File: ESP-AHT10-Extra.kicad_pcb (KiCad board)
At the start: 2 copper layers, 38.2 x 20.8 mm, 23 parts, among them J1 USB, SW1 RESET, SW2 PROG, U1 CH330N, U2 HT7233, U3 ESP-12, U4 AHT10, U5 USBLC6-2SC6

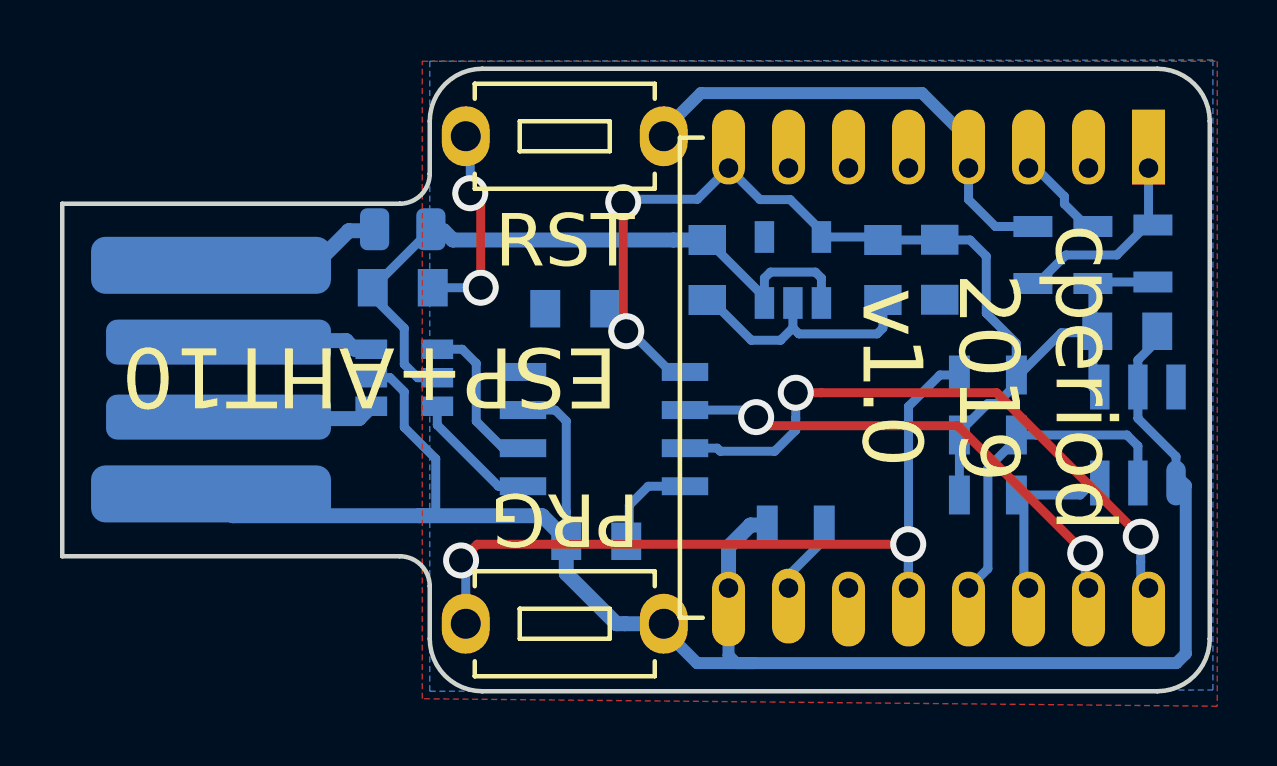
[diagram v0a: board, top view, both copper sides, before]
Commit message: drop vias to 0.6mm
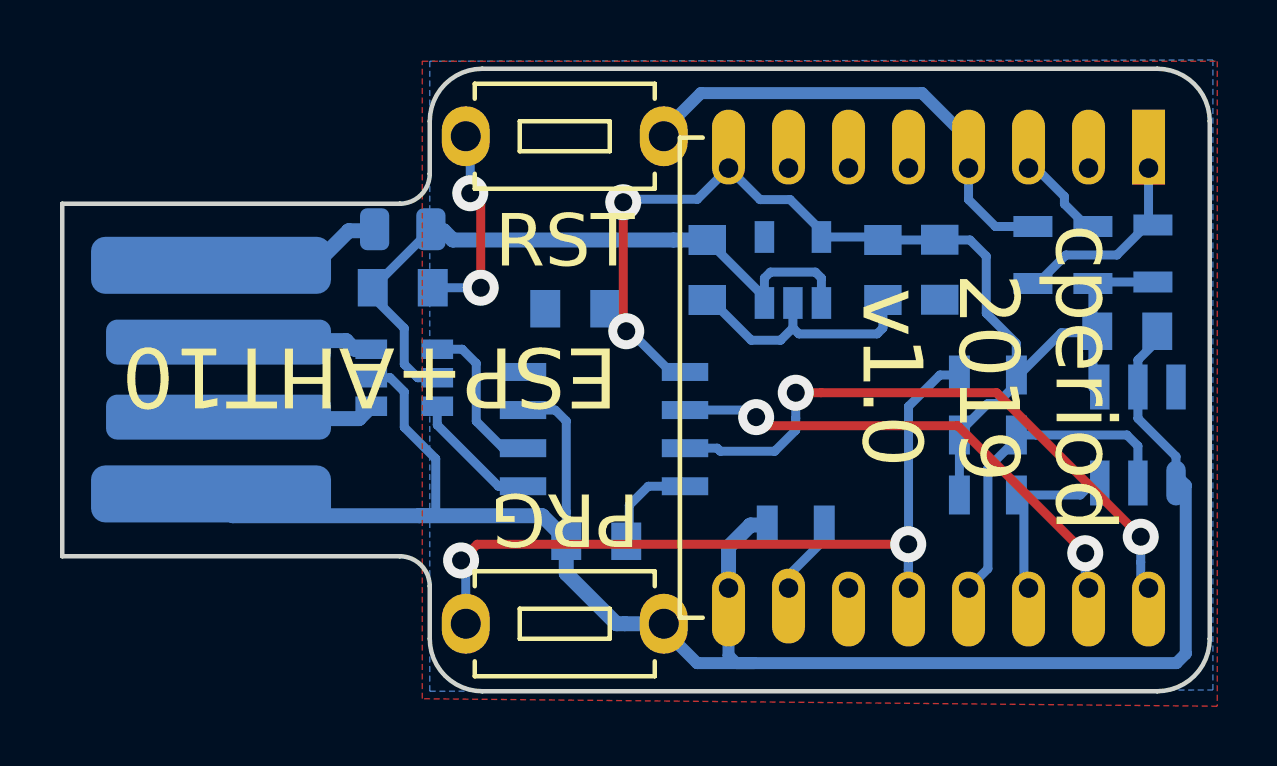
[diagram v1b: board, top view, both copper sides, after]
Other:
- net class Default: via_drill 0.8 -> 0.6
- rule via_min_drill: 0.8 -> 0.6
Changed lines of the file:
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@@
   (page A4)
   (layers
-    (0 F.Cu signal hide)
-    (31 B.Cu signal hide)
-    (32 B.Adhes user hide)
-    (33 F.Adhes user hide)
-    (34 B.Paste user hide)
-    (35 F.Paste user hide)
-    (36 B.SilkS user hide)
-    (37 F.SilkS user hide)
-    (38 B.Mask user hide)
-    (39 F.Mask user hide)
+    (0 F.Cu signal)
+    (31 B.Cu signal)
+    (32 B.Adhes user)
+    (33 F.Adhes user)
+    (34 B.Paste user)
+    (35 F.Paste user)
+    (36 B.SilkS user)
+    (37 F.SilkS user)
+    (38 B.Mask user)
+    (39 F.Mask user)
     (40 Dwgs.User user)
-    (41 Cmts.User user hide)
-    (42 Eco1.User user hide)
-    (43 Eco2.User user hide)
+    (41 Cmts.User user)
+    (42 Eco1.User user)
+    (43 Eco2.User user)
     (44 Edge.Cuts user)
-    (45 Margin user hide)
-    (46 B.CrtYd user hide)
-    (47 F.CrtYd user hide)
-    (48 B.Fab user hide)
-    (49 F.Fab user hide)
+    (45 Margin user)
+    (46 B.CrtYd user)
+    (47 F.CrtYd user)
+    (48 B.Fab user)
+    (49 F.Fab user)
   )
   (setup
@@
     (edge_width 0.15)
     (via_size 1.2)
-    (via_drill 0.8)
+    (via_drill 0.6)
     (via_min_size 1.2)
-    (via_min_drill 0.8)
+    (via_min_drill 0.6)
     (uvia_size 0.3)
     (uvia_drill 0.1)
@@
     (trace_width 0.3)
     (via_dia 1.2)
-    (via_drill 0.8)
+    (via_drill 0.6)
     (uvia_dia 0.3)
     (uvia_drill 0.1)
@@
   (segment (start 157.355703 92.70862) (end 160.25862 92.70862) (width 0.3) (layer B.Cu) (net 1))
   (segment (start 160.25862 92.70862) (end 160.8 93.25) (width 0.3) (layer B.Cu) (net 1))
-  (via (at 148.7 91.45) (size 1.2) (drill 0.8) (layers F.Cu B.Cu) (net 1))
+  (via (at 148.7 91.45) (size 1.2) (drill 0.6) (layers F.Cu B.Cu) (net 1))
   (segment (start 148.8 91.35) (end 148.7 91.45) (width 0.3) (layer B.Cu) (net 1))
   (segment (start 152.209217 90.312374) (end 151.171591 91.35) (width 0.3) (layer B.Cu) (net 1))
   (segment (start 151.171591 91.35) (end 148.8 91.35) (width 0.3) (layer B.Cu) (net 1))
-  (via (at 148.800042 95.75) (size 1.2) (drill 0.8) (layers F.Cu B.Cu) (net 1))
+  (via (at 148.800042 95.75) (size 1.2) (drill 0.6) (layers F.Cu B.Cu) (net 1))
   (segment (start 148.7 91.45) (end 148.7 95.649958) (width 0.3) (layer F.Cu) (net 1))
   (segment (start 148.7 95.649958) (end 148.800042 95.75) (width 0.3) (layer F.Cu) (net 1))
@@
   (segment (start 152.209217 104.312374) (end 152.209217 102.940783) (width 0.5) (layer B.Cu) (net 2))
   (segment (start 152.209217 102.940783) (end 152.94138 102.20862) (width 0.5) (layer B.Cu) (net 2))
-  (via (at 143.95 94.3) (size 1.2) (drill 0.8) (layers F.Cu B.Cu) (net 2))
+  (via (at 143.95 94.3) (size 1.2) (drill 0.6) (layers F.Cu B.Cu) (net 2))
   (segment (start 142.35 94.3) (end 143.95 94.3) (width 0.3) (layer B.Cu) (net 2))
-  (via (at 143.6 91.15) (size 1.2) (drill 0.8) (layers F.Cu B.Cu) (net 2))
+  (via (at 143.6 91.15) (size 1.2) (drill 0.6) (layers F.Cu B.Cu) (net 2))
   (segment (start 143.95 94.3) (end 143.95 91.5) (width 0.3) (layer F.Cu) (net 2))
   (segment (start 143.95 91.5) (end 143.6 91.15) (width 0.3) (layer F.Cu) (net 2))
@@
   (segment (start 158.209217 104.312374) (end 158.2 104.303157) (width 0.3) (layer B.Cu) (net 9))
   (segment (start 158.2 103.698528) (end 158.2 102.85) (width 0.3) (layer B.Cu) (net 9))
-  (via (at 158.2 102.85) (size 1.2) (drill 0.8) (layers F.Cu B.Cu) (net 9))
+  (via (at 158.2 102.85) (size 1.2) (drill 0.6) (layers F.Cu B.Cu) (net 9))
   (segment (start 158.2 104.303157) (end 158.2 103.698528) (width 0.3) (layer B.Cu) (net 9))
   (segment (start 158.2 102.85) (end 143.834321 102.85) (width 0.3) (layer F.Cu) (net 9))
@@
   (segment (start 143.45 103.545839) (end 143.294241 103.39008) (width 0.3) (layer B.Cu) (net 9))
   (segment (start 143.45 105.5) (end 143.45 103.545839) (width 0.3) (layer B.Cu) (net 9))
-  (via (at 143.294241 103.39008) (size 1.2) (drill 0.8) (layers F.Cu B.Cu) (net 9))
+  (via (at 143.294241 103.39008) (size 1.2) (drill 0.6) (layers F.Cu B.Cu) (net 9))
   (segment (start 161.805703 99.35862) (end 161.805703 99.20862) (width 0.3) (layer B.Cu) (net 10))
   (segment (start 160.855703 100.30862) (end 161.805703 99.35862) (width 0.3) (layer B.Cu) (net 10))
@@
   (segment (start 161.805703 101.20862) (end 163.935703 101.20862) (width 0.3) (layer B.Cu) (net 11))
   (segment (start 163.935703 101.20862) (end 164.585703 100.55862) (width 0.3) (layer B.Cu) (net 11))
-  (via (at 164.1 103.15) (size 1.2) (drill 0.8) (layers F.Cu B.Cu) (net 12))
+  (via (at 164.1 103.15) (size 1.2) (drill 0.6) (layers F.Cu B.Cu) (net 12))
   (segment (start 164.1 104.203157) (end 164.209217 104.312374) (width 0.3) (layer B.Cu) (net 12))
   (segment (start 164.1 103.15) (end 164.1 104.203157) (width 0.3) (layer B.Cu) (net 12))
@@
   (segment (start 164.1 103.15) (end 159.850002 98.900002) (width 0.3) (layer F.Cu) (net 12))
   (segment (start 153.417564 98.900002) (end 153.12992 98.612358) (width 0.3) (layer F.Cu) (net 12))
-  (via (at 153.12992 98.612358) (size 1.2) (drill 0.8) (layers F.Cu B.Cu) (net 12))
+  (via (at 153.12992 98.612358) (size 1.2) (drill 0.6) (layers F.Cu B.Cu) (net 12))
   (segment (start 165.95 103.448528) (end 165.95 102.6) (width 0.3) (layer B.Cu) (net 13))
   (segment (start 165.95 104.053157) (end 165.95 103.448528) (width 0.3) (layer B.Cu) (net 13))
   (segment (start 166.209217 104.312374) (end 165.95 104.053157) (width 0.3) (layer B.Cu) (net 13))
-  (via (at 165.95 102.6) (size 1.2) (drill 0.8) (layers F.Cu B.Cu) (net 13))
+  (via (at 165.95 102.6) (size 1.2) (drill 0.6) (layers F.Cu B.Cu) (net 13))
   (segment (start 154.45 99.048528) (end 154.45 98.648528) (width 0.3) (layer B.Cu) (net 13))
   (segment (start 161.15 97.8) (end 155.298528 97.8) (width 0.3) (layer F.Cu) (net 13))
@@
   (segment (start 155.298528 97.8) (end 154.45 97.8) (width 0.3) (layer F.Cu) (net 13))
   (segment (start 151.936845 99.750002) (end 153.748526 99.750002) (width 0.3) (layer B.Cu) (net 13))
-  (via (at 154.45 97.8) (size 1.2) (drill 0.8) (layers F.Cu B.Cu) (net 13))
+  (via (at 154.45 97.8) (size 1.2) (drill 0.6) (layers F.Cu B.Cu) (net 13))
   (segment (start 150.759217 99.647374) (end 151.834217 99.647374) (width 0.3) (layer B.Cu) (net 13))
   (segment (start 134.959217 93.552374) (end 138.397626 93.552374) (width 0.5) (layer B.Cu) (net 14))

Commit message: fix V3 connections to CH330N, bump the bulk caps to 10uF, rev number
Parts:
- C2: value 1u -> 10u
- C4: value 2.2u -> 10u
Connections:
- C6 pad 1: Net-(C6-Pad1) -> 3V3
- U1 pad 8: Net-(C6-Pad1) -> 3V3
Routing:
- net 3V3: track 40.0 -> 49.7 mm
- net Net-(C6-Pad1): track 3.35 -> 0.00 mm
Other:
- board text added: "cperiod 2019 v1.2"
- board text removed: "cperiod 2019 v1.0"
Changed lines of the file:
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@@
     (thickness 1.6)
     (drawings 18)
-    (tracks 201)
+    (tracks 203)
     (zones 0)
     (modules 23)
-    (nets 19)
+    (nets 18)
   )
   (page A4)
@@
   (net 15 UDP+)
   (net 16 UDP-)
-  (net 17 "Net-(C6-Pad1)")
-  (net 18 5V)
+  (net 17 5V)
   (net_class Default "This is the default net class."
     (clearance 0.35)
@@
     (add_net 5V)
     (add_net GND)
-    (add_net "Net-(C6-Pad1)")
     (add_net "Net-(R1-Pad2)")
     (add_net "Net-(R2-Pad1)")
@@
       (effects (font (size 1 1) (thickness 0.15)) (justify mirror))
     )
-    (fp_text value 1u (at -8.10862 0.3 270) (layer B.Fab)
+    (fp_text value 10u (at -8.45862 -0.25 270) (layer B.Fab)
       (effects (font (size 1 1) (thickness 0.15)) (justify mirror))
     )
@@
       (net 2 GND))
     (pad 1 smd rect (at -1 0 270) (size 1 1.25) (layers B.Cu B.Paste B.Mask)
-      (net 18 5V))
+      (net 17 5V))
     (model Capacitors_SMD.3dshapes/C_0805.wrl
       (at (xyz 0 0 0))
@@
       (effects (font (size 1 1) (thickness 0.15)) (justify mirror))
     )
-    (fp_text value 2.2u (at -8.75 0.25 270) (layer B.Fab)
+    (fp_text value 10u (at -8.75 0.25 270) (layer B.Fab)
       (effects (font (size 1 1) (thickness 0.15)) (justify mirror))
     )
@@
       (net 13 eTX))
     (pad 8 smd rect (at 2.7 1.905) (size 1.55 0.6) (layers B.Cu B.Paste B.Mask)
-      (net 17 "Net-(C6-Pad1)"))
+      (net 1 3V3))
     (model ${KISYS3DMOD}/Package_SO.3dshapes/SOIC-8_3.9x4.9mm_P1.27mm.wrl
       (at (xyz 0 0 0))
@@
     (fp_line (start 0.9 1.55) (end 0.9 -1.55) (layer B.Fab) (width 0.1))
     (pad 1 smd rect (at -1.1 0.95 90) (size 1.06 0.65) (layers B.Cu B.Paste B.Mask)
-      (net 18 5V))
+      (net 17 5V))
     (pad 2 smd rect (at -1.1 0 90) (size 1.06 0.65) (layers B.Cu B.Paste B.Mask)
       (net 2 GND))
     (pad 3 smd rect (at -1.1 -0.95 90) (size 1.06 0.65) (layers B.Cu B.Paste B.Mask)
-      (net 18 5V))
+      (net 17 5V))
     (pad 4 smd rect (at 1.1 -0.95 90) (size 1.06 0.65) (layers B.Cu B.Paste B.Mask))
     (pad 5 smd rect (at 1.1 0.95 90) (size 1.06 0.65) (layers B.Cu B.Paste B.Mask)
@@
       (net 2 GND))
     (pad 1 smd rect (at -1 0 180) (size 1 1.25) (layers B.Cu B.Paste B.Mask)
-      (net 17 "Net-(C6-Pad1)"))
+      (net 1 3V3))
     (model Capacitors_SMD.3dshapes/C_0805.wrl
       (at (xyz 0 0 0))
@@
       (net 15 UDP+))
     (pad 5 smd rect (at 1.1 0) (size 1.06 0.65) (layers B.Cu B.Paste B.Mask)
-      (net 18 5V))
+      (net 17 5V))
     (model ${KISYS3DMOD}/Package_TO_SOT_SMD.3dshapes/SOT-23-6.wrl
       (at (xyz 0 0 0))
@@
       (net 14 VBUS))
     (pad 1 smd roundrect (at -0.9375 0 180) (size 0.975 1.4) (layers B.Cu B.Paste B.Mask) (roundrect_rratio 0.25)
-      (net 18 5V))
+      (net 17 5V))
     (model ${KISYS3DMOD}/Fuse.3dshapes/Fuse_0805_2012Metric.wrl
       (at (xyz 0 0 0))
@@
       (net 2 GND))
     (pad 1 smd rect (at -1 0) (size 1 1.25) (layers B.Cu B.Paste B.Mask)
-      (net 18 5V))
+      (net 17 5V))
     (model Capacitors_SMD.3dshapes/C_0805.wrl
       (at (xyz 0 0 0))
@@
   (gr_line (start 130 103.25) (end 130 91.5) (layer Edge.Cuts) (width 0.15))
   (gr_line (start 141.25 103.25) (end 130 103.25) (layer Edge.Cuts) (width 0.15))
-  (gr_text "cperiod\n2019\nv1.0" (at 160.85 97.3 270) (layer F.SilkS)
+  (gr_text "cperiod\n2019\nv1.2" (at 160.85 97.3 270) (layer F.SilkS)
     (effects (font (size 2 2) (thickness 0.3)))
   )
@@
   (segment (start 143.8 98.75) (end 144.697374 99.647374) (width 0.3) (layer B.Cu) (net 16))
   (segment (start 143.33 96.35) (end 143.8 96.82) (width 0.3) (layer B.Cu) (net 16))
-  (segment (start 150.705703 100.970888) (end 150.759217 100.917374) (width 0.3) (layer B.Cu) (net 17))
-  (segment (start 149.532626 100.917374) (end 148.9 101.55) (width 0.3) (layer B.Cu) (net 17))
-  (segment (start 150.759217 100.917374) (end 149.532626 100.917374) (width 0.3) (layer B.Cu) (net 17))
-  (segment (start 148.9 101.55) (end 148.9 102.7) (width 0.3) (layer B.Cu) (net 17))
-  (segment (start 153.405703 94.614323) (end 153.405703 94.80862) (width 0.3) (layer B.Cu) (net 18))
-  (segment (start 151.5 92.70862) (end 153.405703 94.614323) (width 0.3) (layer B.Cu) (net 18))
-  (segment (start 155.105702 93.778619) (end 155.305703 93.97862) (width 0.3) (layer B.Cu) (net 18))
-  (segment (start 153.605704 93.778619) (end 155.105702 93.778619) (width 0.3) (layer B.Cu) (net 18))
-  (segment (start 155.305703 93.97862) (end 155.305703 94.80862) (width 0.3) (layer B.Cu) (net 18))
-  (segment (start 153.405703 93.97862) (end 153.605704 93.778619) (width 0.3) (layer B.Cu) (net 18))
-  (segment (start 153.405703 94.80862) (end 153.405703 93.97862) (width 0.3) (layer B.Cu) (net 18))
-  (segment (start 150.375 92.70862) (end 151.5 92.70862) (width 0.5) (layer B.Cu) (net 18))
-  (segment (start 142.125 92.4) (end 142.7125 92.4) (width 0.5) (layer B.Cu) (net 18))
-  (segment (start 142.7125 92.4) (end 143.02112 92.70862) (width 0.5) (layer B.Cu) (net 18))
-  (segment (start 143.02112 92.70862) (end 150.375 92.70862) (width 0.5) (layer B.Cu) (net 18))
-  (segment (start 142.125 92.525) (end 142.125 92.4) (width 0.3) (layer B.Cu) (net 18))
-  (segment (start 140.35 94.3) (end 142.125 92.525) (width 0.3) (layer B.Cu) (net 18))
-  (segment (start 141.4 95.65) (end 140.5 94.75) (width 0.3) (layer B.Cu) (net 18))
-  (segment (start 141.4 96.85) (end 141.4 95.65) (width 0.3) (layer B.Cu) (net 18))
-  (segment (start 140.5 94.75) (end 140.5 94.3) (width 0.3) (layer B.Cu) (net 18))
-  (segment (start 142.5 97.3) (end 141.85 97.3) (width 0.3) (layer B.Cu) (net 18))
-  (segment (start 141.85 97.3) (end 141.4 96.85) (width 0.3) (layer B.Cu) (net 18))
+  (segment (start 150.705703 100.970888) (end 150.759217 100.917374) (width 0.3) (layer B.Cu) (net 1))
+  (segment (start 150.759217 100.917374) (end 150.582626 100.917374) (width 0.3) (layer B.Cu) (net 1))
+  (segment (start 148.9 102.6) (end 148.9 102.7) (width 0.3) (layer B.Cu) (net 1))
+  (segment (start 150.582626 100.917374) (end 148.9 102.6) (width 0.3) (layer B.Cu) (net 1))
+  (segment (start 148.8 95.750042) (end 148.800042 95.75) (width 0.3) (layer B.Cu) (net 1))
+  (segment (start 148.8 102.75) (end 148.8 95.750042) (width 0.3) (layer B.Cu) (net 1))
+  (segment (start 153.405703 94.614323) (end 153.405703 94.80862) (width 0.3) (layer B.Cu) (net 17))
+  (segment (start 151.5 92.70862) (end 153.405703 94.614323) (width 0.3) (layer B.Cu) (net 17))
+  (segment (start 155.105702 93.778619) (end 155.305703 93.97862) (width 0.3) (layer B.Cu) (net 17))
+  (segment (start 153.605704 93.778619) (end 155.105702 93.778619) (width 0.3) (layer B.Cu) (net 17))
+  (segment (start 155.305703 93.97862) (end 155.305703 94.80862) (width 0.3) (layer B.Cu) (net 17))
+  (segment (start 153.405703 93.97862) (end 153.605704 93.778619) (width 0.3) (layer B.Cu) (net 17))
+  (segment (start 153.405703 94.80862) (end 153.405703 93.97862) (width 0.3) (layer B.Cu) (net 17))
+  (segment (start 150.375 92.70862) (end 151.5 92.70862) (width 0.5) (layer B.Cu) (net 17))
+  (segment (start 142.125 92.4) (end 142.7125 92.4) (width 0.5) (layer B.Cu) (net 17))
+  (segment (start 142.7125 92.4) (end 143.02112 92.70862) (width 0.5) (layer B.Cu) (net 17))
+  (segment (start 143.02112 92.70862) (end 150.375 92.70862) (width 0.5) (layer B.Cu) (net 17))
+  (segment (start 142.125 92.525) (end 142.125 92.4) (width 0.3) (layer B.Cu) (net 17))
+  (segment (start 140.35 94.3) (end 142.125 92.525) (width 0.3) (layer B.Cu) (net 17))
+  (segment (start 141.4 95.65) (end 140.5 94.75) (width 0.3) (layer B.Cu) (net 17))
+  (segment (start 141.4 96.85) (end 141.4 95.65) (width 0.3) (layer B.Cu) (net 17))
+  (segment (start 140.5 94.75) (end 140.5 94.3) (width 0.3) (layer B.Cu) (net 17))
+  (segment (start 142.5 97.3) (end 141.85 97.3) (width 0.3) (layer B.Cu) (net 17))
+  (segment (start 141.85 97.3) (end 141.4 96.85) (width 0.3) (layer B.Cu) (net 17))
   (zone (net 0) (net_name "") (layers F&B.Cu) (hatch edge 0.508)
     (connect_pads (clearance 0.508))
